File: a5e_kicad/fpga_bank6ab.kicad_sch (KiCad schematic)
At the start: 1 part, among them U7 A5EB013B-B23B

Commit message: Schematic reorg step 9: ERC to zero
- Wires trimmed back to their last label or cap (SDM config lines, LPDDR4
  decoupling rows, PG pins); loose stubs and R29 leftovers removed
- Unused bus links removed: {iob6a}, {iobank_2aB}, {iob6c}, {phy} and the
  io_headers {jtag} (sheet pins, root buses, unnamed internal buses);
  {iob6b} bus tail trimmed

Netdiff: 0 renamed, 0 connectivity diffs. ERC 21 -> 0. PCB unchanged, DRC parity 0.
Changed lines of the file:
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@@
-	(bus
-		(pts
-			(xy 50.8 22.86) (xy 66.04 22.86)
-		)
-		(stroke
-			(width 0)
-			(type default)
-		)
-	)
 	(bus
 		(pts
@@
 		)
 	)
-	(bus
-		(pts
-			(xy 66.04 71.12) (xy 66.04 73.66)
-		)
-		(stroke
-			(width 0)
-			(type default)
-		)
-	)
-	(bus
-		(pts
-			(xy 66.04 73.66) (xy 66.04 76.2)
-		)
-		(stroke
-			(width 0)
-			(type default)
-		)
-	)
 	(wire
 		(pts
@@
 	(bus
 		(pts
-			(xy 66.04 35.56) (xy 66.04 38.1)
-		)
-		(stroke
-			(width 0)
-			(type default)
-		)
-	)
-	(bus
-		(pts
 			(xy 66.04 81.28) (xy 66.04 83.82)
 		)
@@
 		)
 	)
-	(bus
-		(pts
-			(xy 66.04 38.1) (xy 66.04 40.64)
-		)
-		(stroke
-			(width 0)
-			(type default)
-		)
-	)
 	(wire
 		(pts
@@
 	(bus
 		(pts
-			(xy 66.04 30.48) (xy 66.04 33.02)
-		)
-		(stroke
-			(width 0)
-			(type default)
-		)
-	)
-	(bus
-		(pts
 			(xy 66.04 88.9) (xy 66.04 91.44)
 		)
@@
 	(bus
 		(pts
-			(xy 66.04 45.72) (xy 66.04 50.8)
-		)
-		(stroke
-			(width 0)
-			(type default)
-		)
-	)
-	(bus
-		(pts
 			(xy 66.04 116.84) (xy 66.04 121.92)
 		)
@@
 		)
 	)
-	(bus
-		(pts
-			(xy 66.04 50.8) (xy 66.04 53.34)
-		)
-		(stroke
-			(width 0)
-			(type default)
-		)
-	)
 	(wire
 		(pts
@@
 	(bus
 		(pts
-			(xy 66.04 25.4) (xy 66.04 27.94)
-		)
-		(stroke
-			(width 0)
-			(type default)
-		)
-	)
-	(bus
-		(pts
 			(xy 66.04 104.14) (xy 66.04 106.68)
 		)
@@
 	(bus
 		(pts
-			(xy 66.04 68.58) (xy 66.04 71.12)
-		)
-		(stroke
-			(width 0)
-			(type default)
-		)
-	)
-	(bus
-		(pts
 			(xy 66.04 124.46) (xy 66.04 132.08)
 		)
@@
 		)
 	)
-	(bus
-		(pts
-			(xy 66.04 60.96) (xy 66.04 63.5)
-		)
-		(stroke
-			(width 0)
-			(type default)
-		)
-	)
-	(bus
-		(pts
-			(xy 66.04 55.88) (xy 66.04 58.42)
-		)
-		(stroke
-			(width 0)
-			(type default)
-		)
-	)
-	(bus
-		(pts
-			(xy 66.04 33.02) (xy 66.04 35.56)
-		)
-		(stroke
-			(width 0)
-			(type default)
-		)
-	)
-	(bus
-		(pts
-			(xy 66.04 58.42) (xy 66.04 60.96)
-		)
-		(stroke
-			(width 0)
-			(type default)
-		)
-	)
-	(bus
-		(pts
-			(xy 66.04 53.34) (xy 66.04 55.88)
-		)
-		(stroke
-			(width 0)
-			(type default)
-		)
-	)
 	(wire
 		(pts
@@
 		)
 	)
-	(bus
-		(pts
-			(xy 66.04 27.94) (xy 66.04 30.48)
-		)
-		(stroke
-			(width 0)
-			(type default)
-		)
-	)
-	(bus
-		(pts
-			(xy 66.04 22.86) (xy 66.04 25.4)
-		)
-		(stroke
-			(width 0)
-			(type default)
-		)
-	)
 	(wire
 		(pts
@@
 	(bus
 		(pts
-			(xy 66.04 40.64) (xy 66.04 43.18)
-		)
-		(stroke
-			(width 0)
-			(type default)
-		)
-	)
-	(bus
-		(pts
-			(xy 66.04 66.04) (xy 66.04 68.58)
-		)
-		(stroke
-			(width 0)
-			(type default)
-		)
-	)
-	(bus
-		(pts
 			(xy 66.04 132.08) (xy 66.04 134.62)
 		)
@@
 	(bus
 		(pts
-			(xy 66.04 63.5) (xy 66.04 66.04)
-		)
-		(stroke
-			(width 0)
-			(type default)
-		)
-	)
-	(bus
-		(pts
 			(xy 66.04 83.82) (xy 66.04 86.36)
-		)
-		(stroke
-			(width 0)
-			(type default)
-		)
-	)
-	(bus
-		(pts
-			(xy 66.04 43.18) (xy 66.04 45.72)
 		)
 		(stroke
@@
 		)
 	)
-	(hierarchical_label "{iob6a}"
-		(shape bidirectional)
-		(at 50.8 22.86 180)
-		(effects
-			(font
-				(size 1.27 1.27)
-			)
-			(justify right)
-		)
-	)

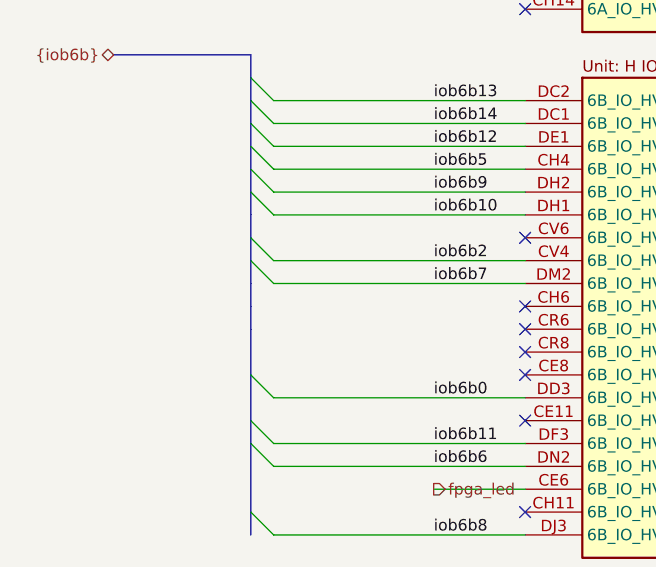
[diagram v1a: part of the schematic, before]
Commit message: Ethernet PHY passives to 0201, R27/R28 to 0402, preliminary RGMII routing
- 31 PHY passives on the hps_ethernet sheet 0402 -> 0201 (C24 22u stays
  0402): 100n C190183, 1u C272877, 27p C85899, 10k C473048,
  330R C516485, 4K7 C270346, 1K5 C270361, 2K49 C473476.
- Refclk bias R27/R28 0201 -> 0402 (C25120, 49.9R); R28 moved 0.1 mm
  to +x to clear the refclk_N meander.
- Preliminary RGMII routing: RX on F.Cu, TX on In2. Group spread
  TX 79 ps (TXD1 longest), RX 44 ps.
- Schematic sheets as saved by eeschema.
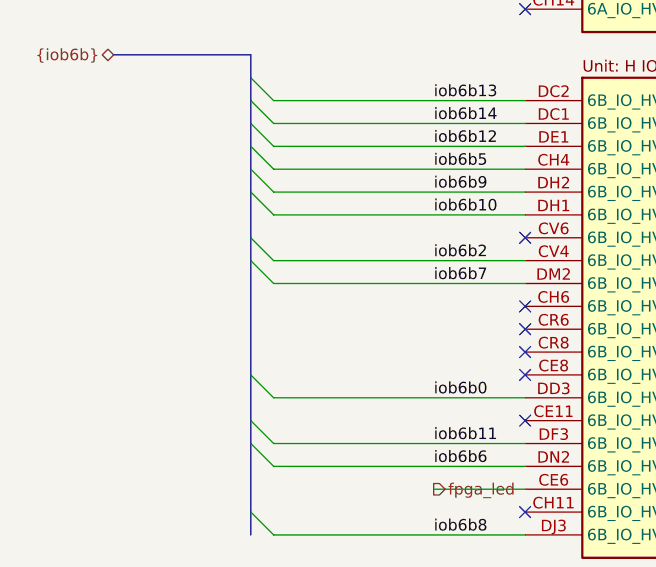
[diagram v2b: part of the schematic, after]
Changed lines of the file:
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@@
 	)
 	(no_connect
+		(at 96.52 71.12)
+	)
+	(no_connect
+		(at 96.52 73.66)
+	)
+	(no_connect
+		(at 96.52 40.64)
+	)
+	(no_connect
+		(at 96.52 63.5)
+	)
+	(no_connect
+		(at 96.52 35.56)
+	)
+	(no_connect
+		(at 96.52 76.2)
+	)
+	(no_connect
+		(at 96.52 48.26)
+	)
+	(no_connect
 		(at 96.52 50.8)
 	)
 	(no_connect
+		(at 96.52 53.34)
+	)
+	(no_connect
 		(at 96.52 116.84)
 	)
 	(no_connect
+		(at 96.52 111.76)
+	)
+	(no_connect
+		(at 96.52 38.1)
+	)
+	(no_connect
+		(at 96.52 33.02)
+	)
+	(no_connect
+		(at 96.52 55.88)
+	)
+	(no_connect
+		(at 96.52 43.18)
+	)
+	(no_connect
+		(at 96.52 109.22)
+	)
+	(no_connect
+		(at 96.52 66.04)
+	)
+	(no_connect
+		(at 96.52 58.42)
+	)
+	(no_connect
+		(at 96.52 101.6)
+	)
+	(no_connect
+		(at 96.52 45.72)
+	)
+	(no_connect
+		(at 96.52 68.58)
+	)
+	(no_connect
+		(at 96.52 27.94)
+	)
+	(no_connect
+		(at 96.52 114.3)
+	)
+	(no_connect
+		(at 96.52 30.48)
+	)
+	(no_connect
 		(at 96.52 132.08)
 	)
+	(no_connect
+		(at 96.52 60.96)
+	)
 	(bus_entry
 		(at 66.04 91.44)
@@
 	(bus
 		(pts
-			(xy 66.04 96.52) (xy 66.04 99.06)
-		)
-		(stroke
-			(width 0)
-			(type default)
-		)
-	)
-	(bus
-		(pts
-			(xy 66.04 99.06) (xy 66.04 101.6)
-		)
-		(stroke
-			(width 0)
-			(type default)
-		)
-	)
-	(bus
-		(pts
-			(xy 66.04 106.68) (xy 66.04 109.22)
+			(xy 66.04 96.52) (xy 66.04 101.6)
 		)
 		(stroke
@@
 		)
 	)
-	(bus
-		(pts
-			(xy 66.04 109.22) (xy 66.04 111.76)
-		)
-		(stroke
-			(width 0)
-			(type default)
-		)
-	)
 	(wire
 		(pts
@@
 	(bus
 		(pts
-			(xy 66.04 104.14) (xy 66.04 106.68)
-		)
-		(stroke
-			(width 0)
-			(type default)
-		)
-	)
-	(bus
-		(pts
 			(xy 66.04 124.46) (xy 66.04 132.08)
 		)
@@
 	(bus
 		(pts
-			(xy 66.04 111.76) (xy 66.04 116.84)
+			(xy 66.04 104.14) (xy 66.04 116.84)
 		)
 		(stroke
@@
 		)
 	)
-	(no_connect
-		(at 96.52 111.76)
-	)
-	(no_connect
-		(at 96.52 53.34)
-	)
-	(no_connect
-		(at 96.52 66.04)
-	)
-	(no_connect
-		(at 96.52 30.48)
-	)
-	(no_connect
-		(at 96.52 109.22)
-	)
-	(no_connect
-		(at 96.52 43.18)
-	)
-	(no_connect
-		(at 96.52 35.56)
-	)
-	(no_connect
-		(at 96.52 58.42)
-	)
-	(no_connect
-		(at 96.52 63.5)
-	)
-	(no_connect
-		(at 96.52 48.26)
-	)
-	(no_connect
-		(at 96.52 68.58)
-	)
-	(no_connect
-		(at 96.52 33.02)
-	)
-	(no_connect
-		(at 96.52 38.1)
-	)
-	(no_connect
-		(at 96.52 71.12)
-	)
-	(no_connect
-		(at 96.52 55.88)
-	)
-	(no_connect
-		(at 96.52 114.3)
-	)
-	(no_connect
-		(at 96.52 40.64)
-	)
-	(no_connect
-		(at 96.52 101.6)
-	)
-	(no_connect
-		(at 96.52 45.72)
-	)
-	(no_connect
-		(at 96.52 60.96)
-	)
-	(no_connect
-		(at 96.52 76.2)
-	)
-	(no_connect
-		(at 96.52 27.94)
-	)
-	(no_connect
-		(at 96.52 73.66)
-	)
 )
